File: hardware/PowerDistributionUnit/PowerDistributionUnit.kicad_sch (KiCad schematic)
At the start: 16 parts, among them J0 Conn_01x02, J1 Conn_01x02, J10 Conn_01x02, J11 Conn_01x02, J12 Conn_01x02, J13 Conn_01x02, J14 Conn_01x02, J16 Conn_01x02, J2 Conn_01x02, J3 Conn_01x02, J4 Conn_01x02, J5 Conn_01x02, J6 Conn_01x02, J7 Conn_01x02, J8 Conn_01x02, J9 Conn_01x02

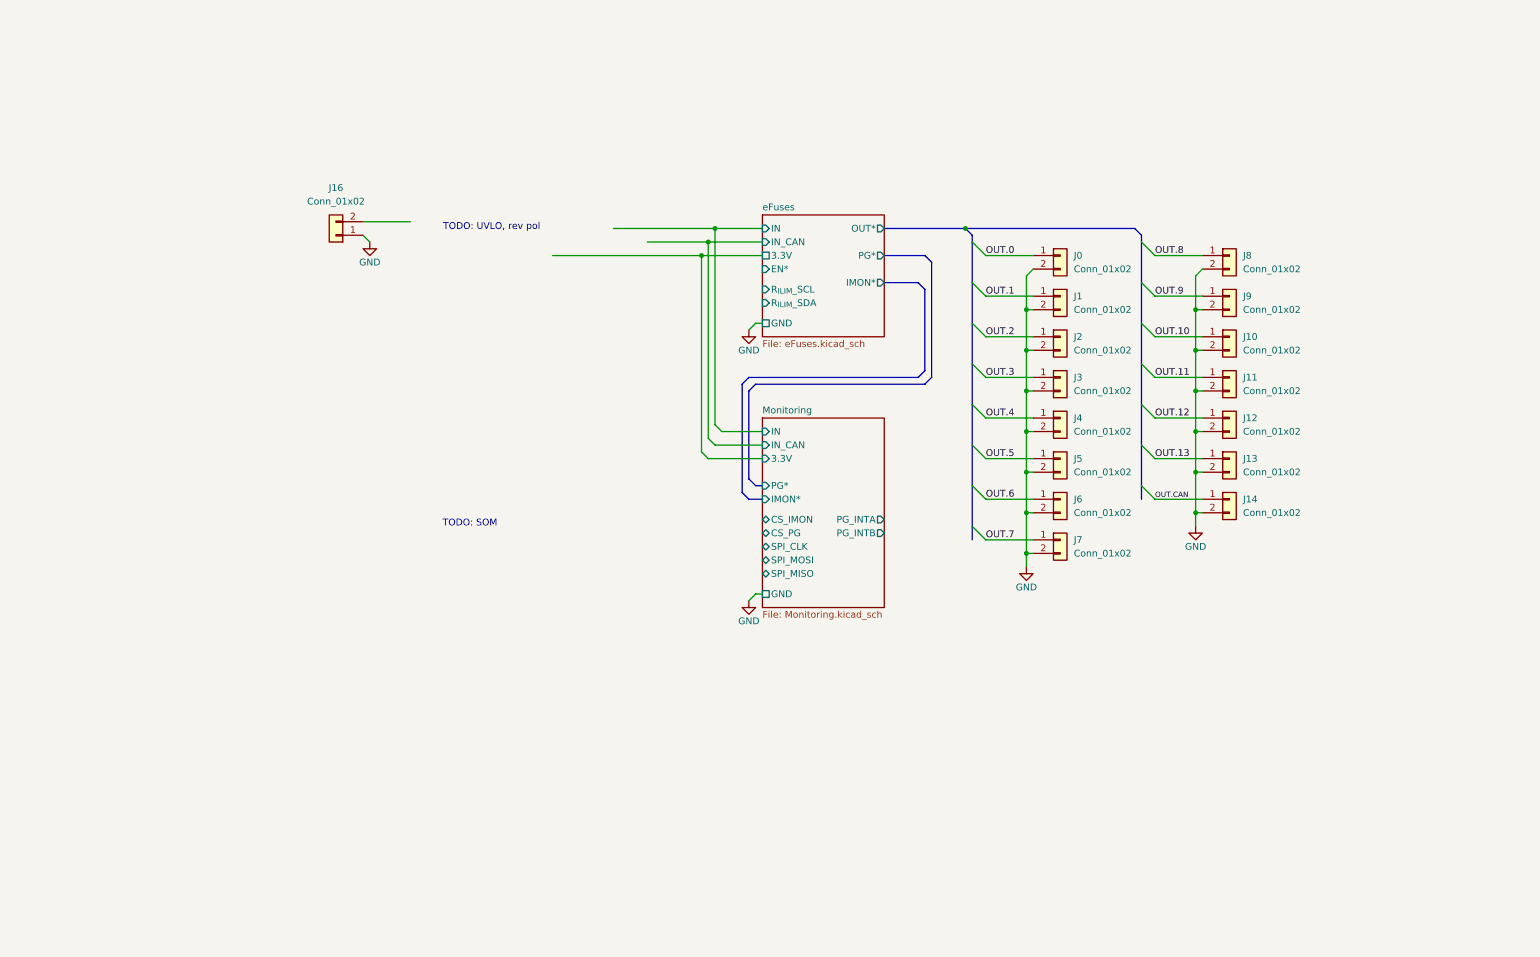
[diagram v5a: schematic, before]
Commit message: added isolated CAN 5V DC-DC converter, updated power netclasses
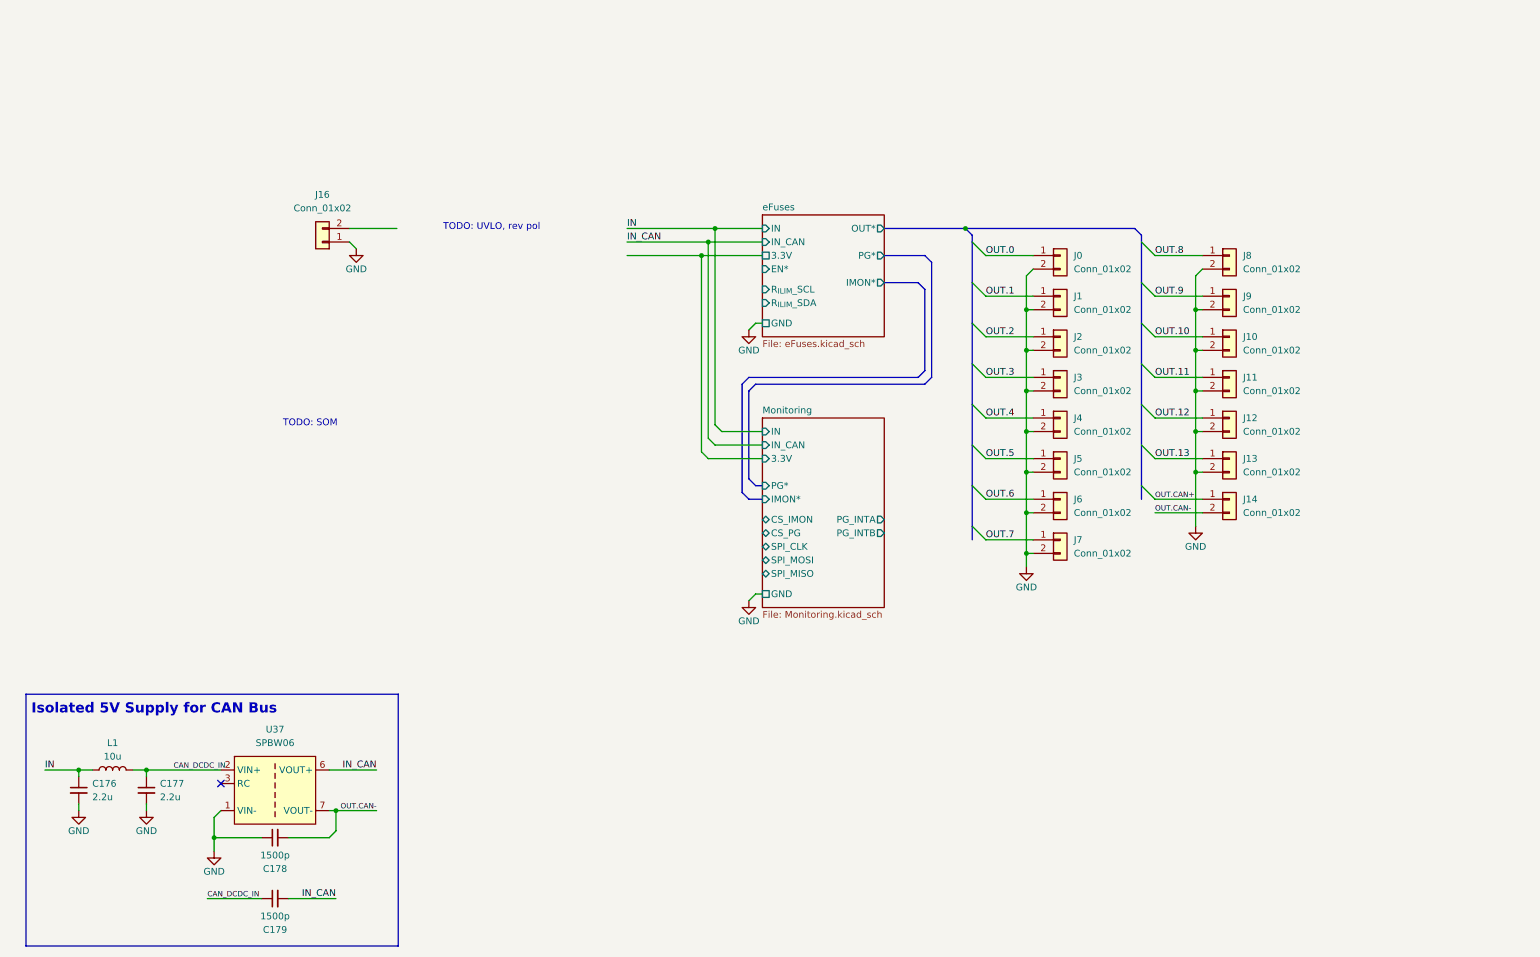
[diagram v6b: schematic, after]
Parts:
- added C176, C177: 2.2u, symbol Device:C_Small
- added C178, C179: 1500p, symbol Device:C_Small
- added L1: 10u, symbol Device:L
- added U37: SPBW06, PowerDistributionUnitLib:SPBW06, symbol PowerDistributionUnitLib:SPBW06F
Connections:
- net GND: now also C176.2, C177.2, C178.1, U37.1 (VIN-); no longer J14.2 (Pin_2)
- net OUT.CAN renamed OUT.CAN+
- new net CAN_DCDC_IN: C177.1, C179.1, L1.2, U37.2 (VIN+)
- new net IN: C176.1, L1.1
- new net IN_CAN: C179.2, U37.6 (VOUT+)
- new net OUT.CAN-: C178.2, J14.2 (Pin_2), U37.7 (VOUT-)
- no-connect marks 0 -> 1
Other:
- note added: "Isolated 5V Supply for CAN Bus"
- moved on the sheet: J16

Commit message: fixed Lakshay review things (CAN DC-DC output caps, DC-DC symbol name update, fix CAN eFuse isolation, add CAN connectors, DC-DC RC jumper, voltage label) and removed PG int from EN mux
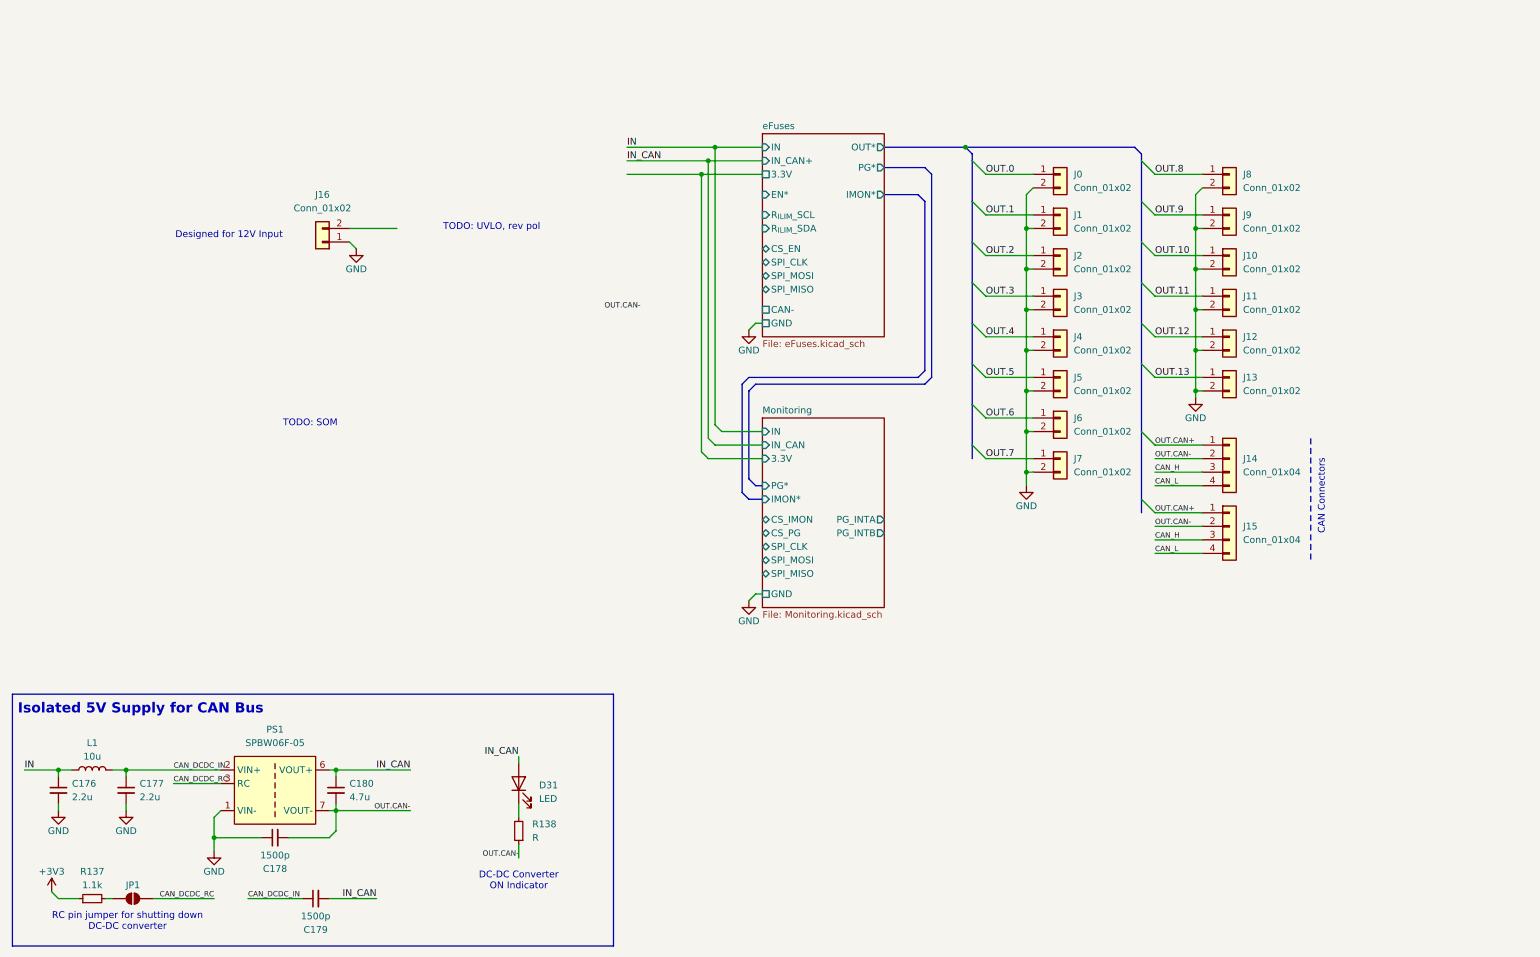
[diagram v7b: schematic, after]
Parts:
- added C180: 4.7u, symbol Device:C_Small
- added D31: LED, symbol Device:LED
- added J15: Conn_01x04, symbol Connector_Generic:Conn_01x04
- added JP1: SolderJumper_2_Open, Jumper:SolderJumper-2_P1.3mm_Open_TrianglePad1.0x1.5mm, symbol Jumper:SolderJumper_2_Open
- added R137: 1.1k, symbol Device:R_Small
- added R138: R, symbol Device:R_Small
- J14: value Conn_01x02 -> Conn_01x04; symbol Connector_Generic:Conn_01x02 -> Connector_Generic:Conn_01x04
- PS1: renamed from U37; value SPBW06 -> SPBW06F-05; footprint PowerDistributionUnitLib:SPBW06 -> PowerDistributionUnitLib:SPBW06F-xx; symbol PowerDistributionUnitLib:SPBW06F -> PowerDistributionUnitLib:SPBW06F-xx
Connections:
- net IN_CAN: now also C180.1, D31.2 (A)
- net OUT.CAN+: now also J15.1 (Pin_1)
- net OUT.CAN-: now also C180.2, J15.2 (Pin_2), R138.1
- net CAN_DCDC_RC: now reaches PS1.3 (RC)
- net CAN_DCDC_RC: now also JP1.2 (B)
- new net: JP1.1 (A), R137.2
- new net: D31.1 (K), R138.2
- new net +3V3: R137.1
- new net CAN_H: J14.3 (Pin_3), J15.3 (Pin_3)
- new net CAN_L: J14.4 (Pin_4), J15.4 (Pin_4)
- no-connect marks 1 -> 0
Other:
- sheet eFuses ports: added CAN-, CS_EN, IN_CAN+, SPI_CLK, SPI_MISO, SPI_MOSI; removed IN_CAN
- note added: "CAN Connectors"
- note added: "DC-DC Converter ON Indicator"
- note added: "Designed for 12V Input"
- note added: "RC pin jumper for shutting down DC-DC converter"
- moved on the sheet: C176, C177, C179, J0, J1, J10, J11, J12, J13, J2, J3, J4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

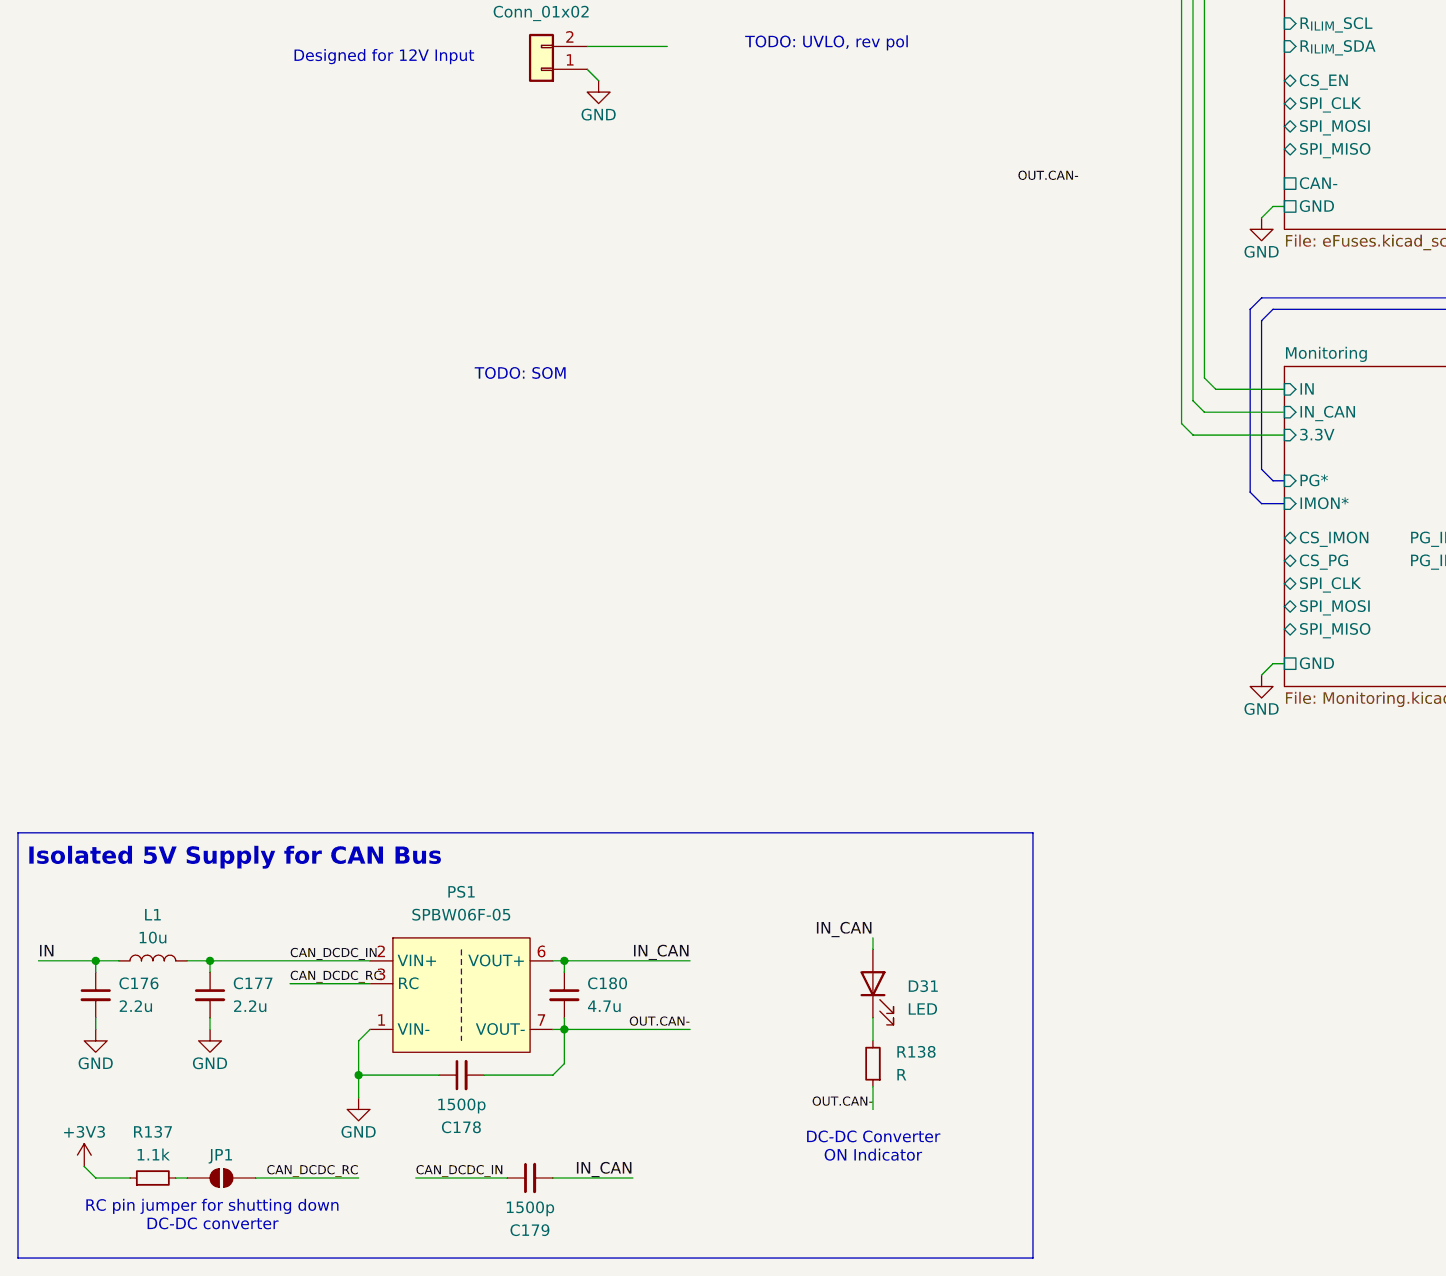
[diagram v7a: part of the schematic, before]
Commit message: Continued revising eFuse isolation. Also fixed pulls on ADCMUX
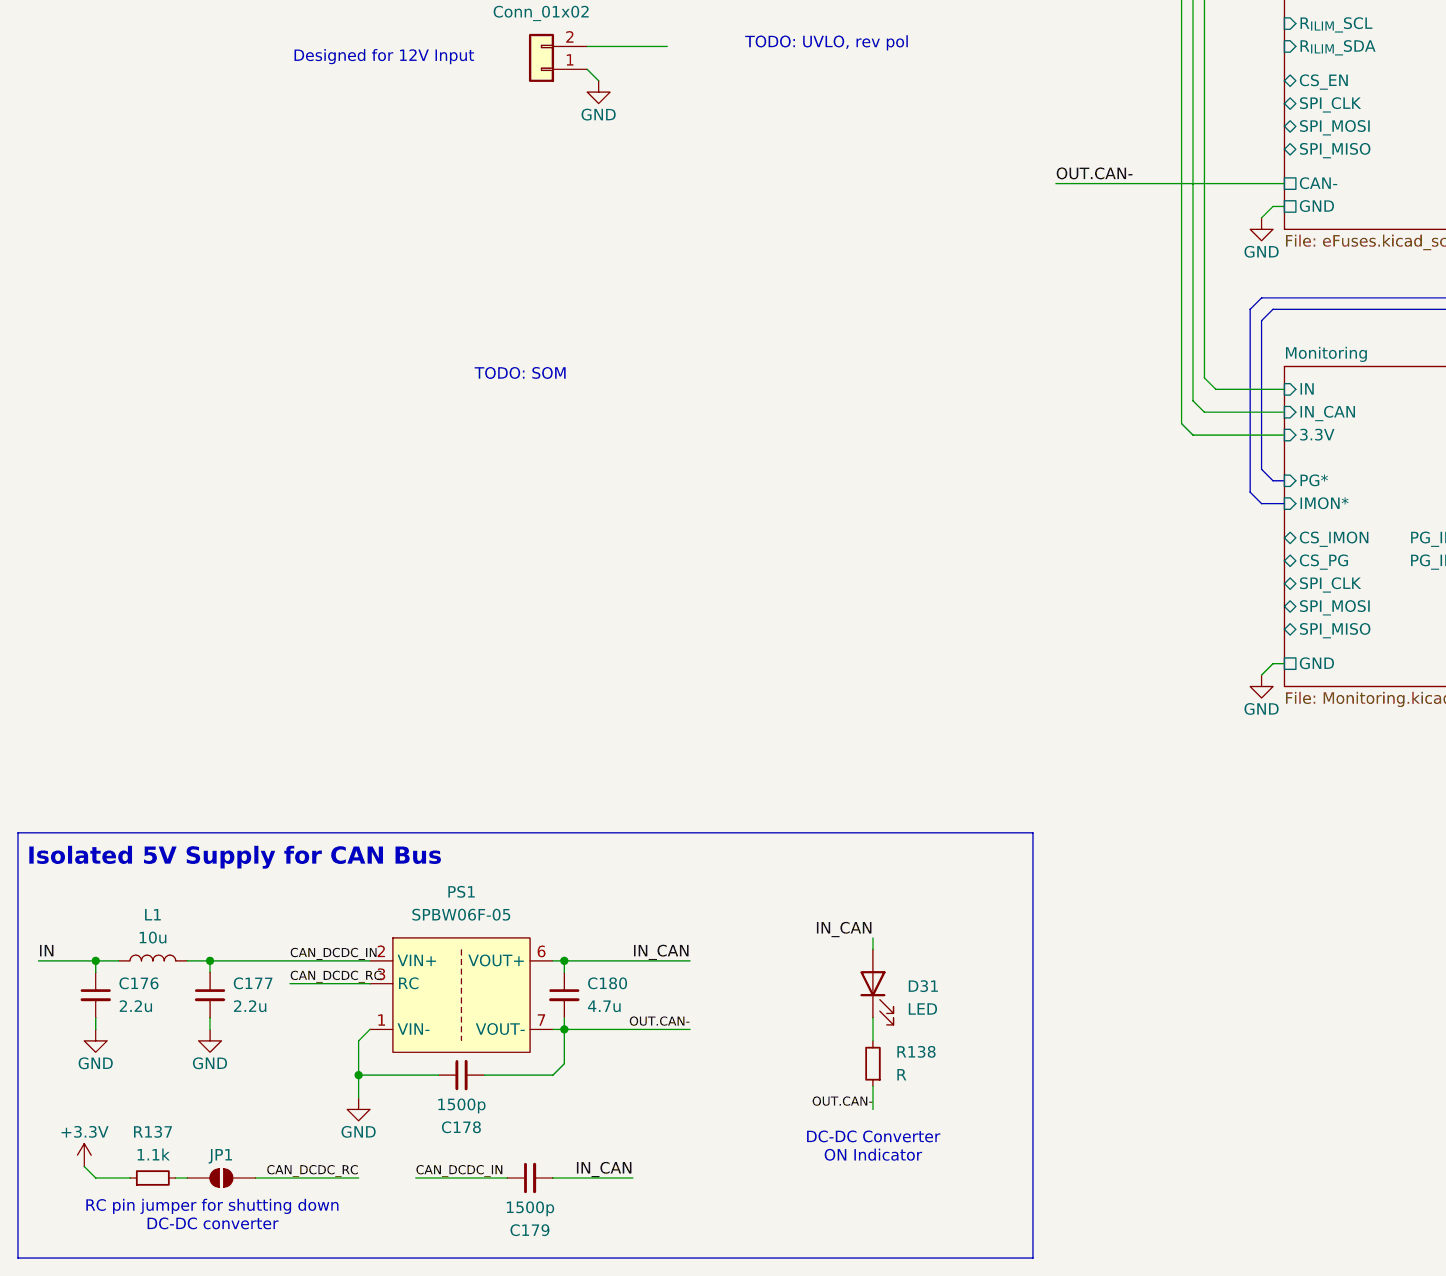
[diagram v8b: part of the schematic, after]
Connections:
- net +3V3 renamed +3.3V
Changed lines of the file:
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@@
 	(wire
 		(pts
+			(xy 133.35 71.12) (xy 158.75 71.12)
+		)
+		(stroke
+			(width 0)
+			(type default)
+			(color 72 72 72 1)
+		)
+	)
+	(wire
+		(pts
 			(xy 240.03 63.5) (xy 241.3 63.5)
 		)
@@
 	)
 	(label "OUT.CAN-"
-		(at 135.89 71.12 180)
+		(at 133.35 71.12 0)
 		(fields_autoplaced yes)
 		(effects
 			(font
-				(size 1 1)
+				(size 1.27 1.27)
 			)
-			(justify right bottom)
+			(justify left bottom)
 		)
 	)
@@
 			)
 		)
-		(property "Value" "+3V3"
+		(property "Value" "+3.3V"
 			(at 25.4 176.53 0)
 			(effects
